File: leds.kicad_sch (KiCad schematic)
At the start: 47 parts, among them Q5 AO3401A, Q7 2N7002, U9 TXB0101DCK

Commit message: added lcsc part numbers
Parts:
- C47, C49, C51, C53, C55, C57, C58, C59, C60, C61, C67, C68, C69, C70, C71, C72, C73, C74, C75, C76: LCSC (none) -> C60474
- D23, D24, D25, D26, D27, D28, D29, D30, D31, D32, D33, D34, D35, D36, D37, D38, D39, D40, D41, D42: LCSC (none) -> C5149201
- Q7: LCSC C916396 -> C916396
- R13, R16, R20: LCSC (none) -> C25744
- R6: LCSC (none) -> C25076

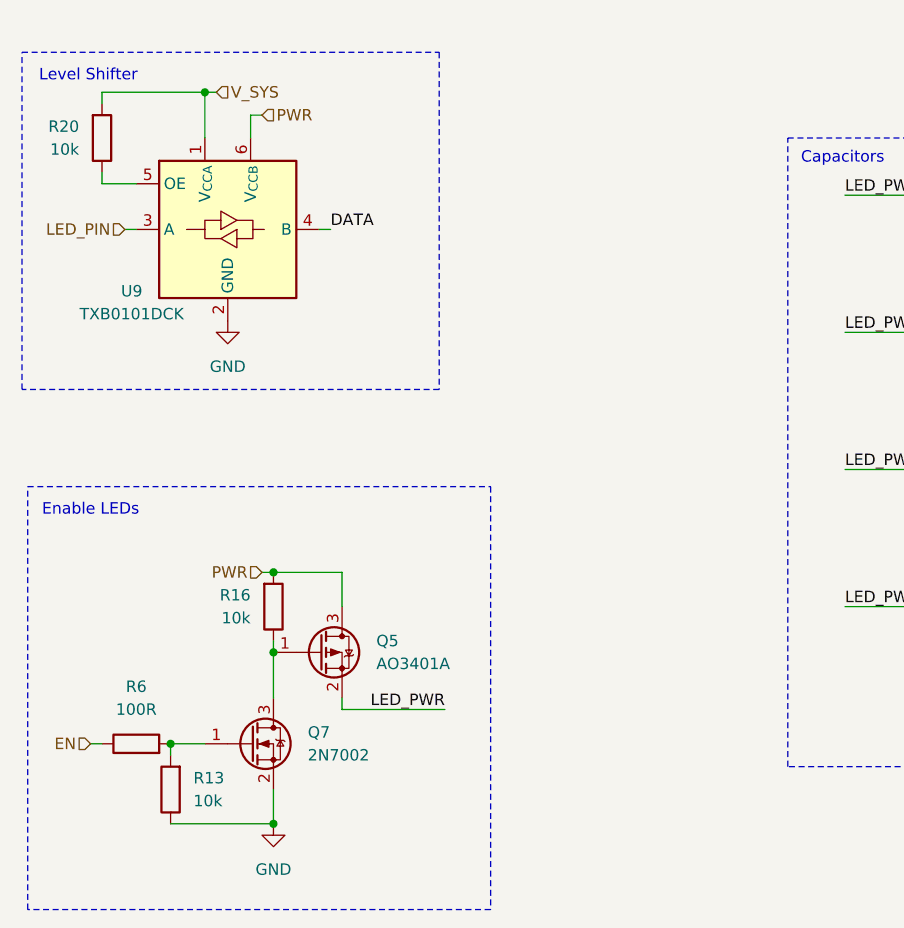
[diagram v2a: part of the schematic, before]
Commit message: fixed fillzones
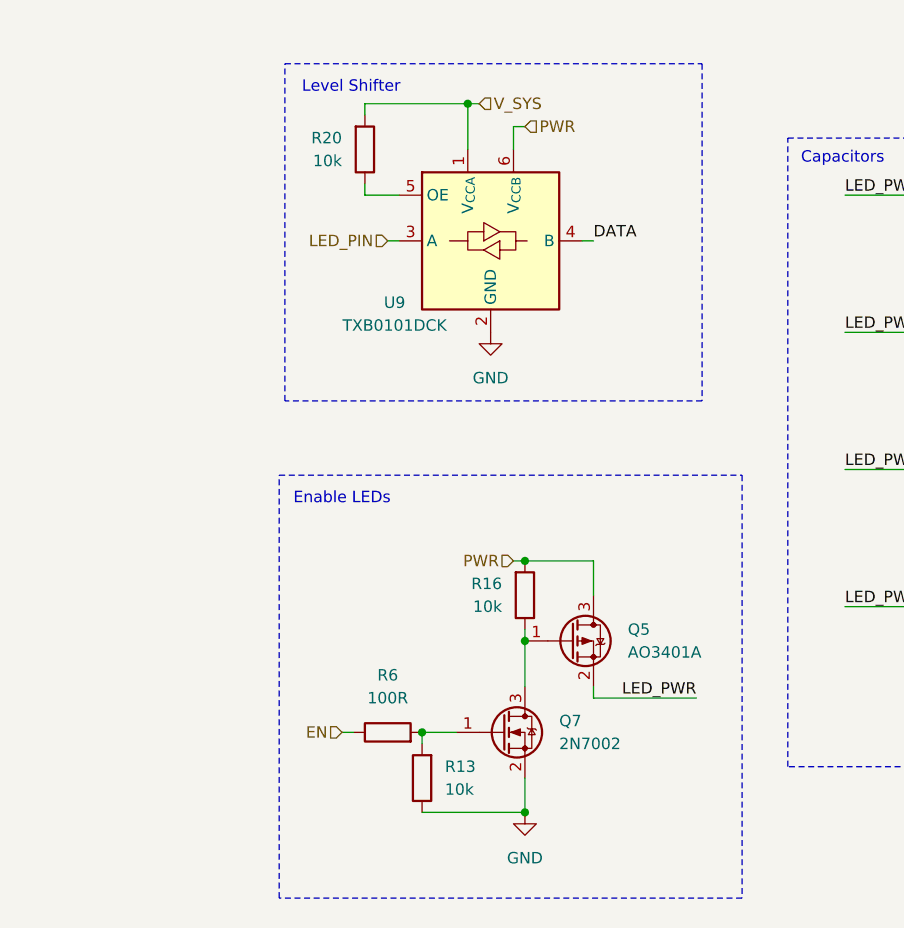
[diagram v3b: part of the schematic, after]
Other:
- moved on the sheet: Q5, Q7, R13, R16, R20, R6, U9
